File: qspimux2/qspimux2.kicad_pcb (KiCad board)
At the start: 4 copper layers, 14.2 x 23.2 mm, 13 parts, among them J101 Conn_01x10_MountingPin, J102 Conn_02x04_Odd_Even, J103 Conn_02x04_Odd_Even, U101 TS3A27518ERTWR, U102 MAX40200AUK, U103 MAX40200AUK

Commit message: qspimux2: rename project files and fix net name bugs
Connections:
- net /IO0_DO_FLASH renamed /IO1_DO_FLASH

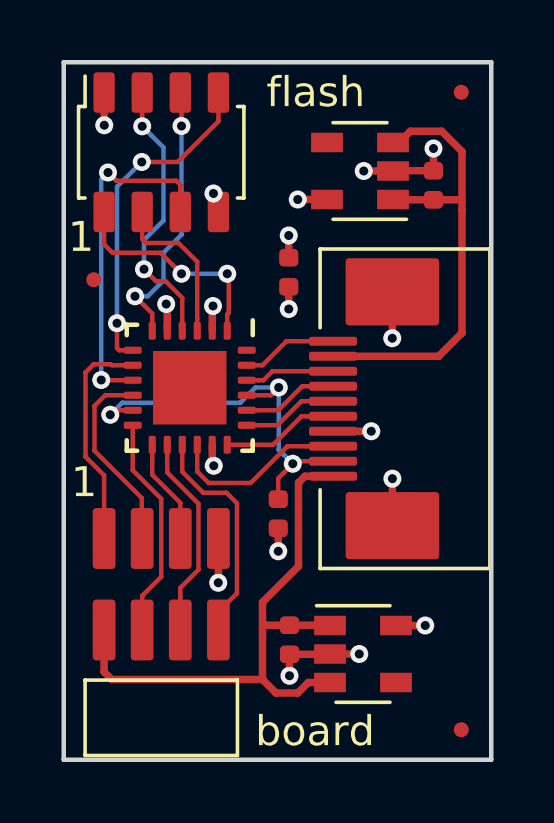
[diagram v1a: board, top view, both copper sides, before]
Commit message: qspimux2: slighty optimize board layout
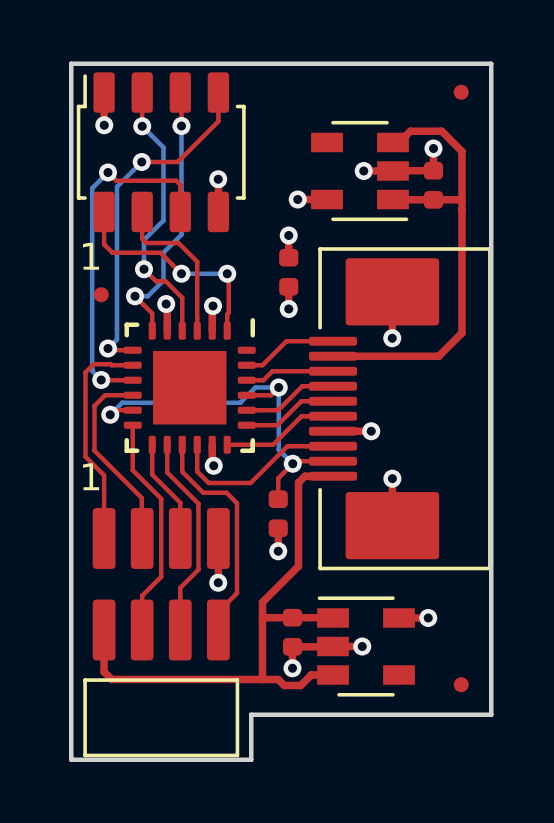
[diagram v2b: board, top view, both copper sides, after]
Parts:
- moved REF** 1.50 mm to (104.2, 68.0)
- moved REF** 0.56 mm to (92.2, 55.0)
- moved U102 0.27 mm to (101.1, 66.7)
- moved C102 0.27 mm to (98.6, 66.2)
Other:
- board size 14.2 x 23.2 mm -> 14 x 23.2 mm

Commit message: qspimux2: rename connectors to match the actual part numbers
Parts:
- J102: footprint qspimux-footprints:CLP-104-02-F-DH-A -> qspimux-footprints:CLP-104-02-F-DH
- J103: footprint qspimux-footprints:FTSH-104-01-F-DH-A -> qspimux-footprints:FTSH-104-01-F-DH
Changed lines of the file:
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@@
     (add_net GND)
   )
-  (module qspimux-footprints:CLP-104-02-F-DH-A (layer F.Cu)
+  (module qspimux-footprints:CLP-104-02-F-DH (layer F.Cu)
     (at 94.25 50.25 180)
     (fp_text reference J102 (at 0 -3.81 180) (layer F.Fab)
@@
       (net 1 GND))
   )
-  (module qspimux-footprints:FTSH-104-01-F-DH-A (layer F.Cu)
+  (module qspimux-footprints:FTSH-104-01-F-DH (layer F.Cu)
     (at 94.25 64.65 180)
     (fp_text reference J103 (at 0 3.81 180) (layer F.Fab)

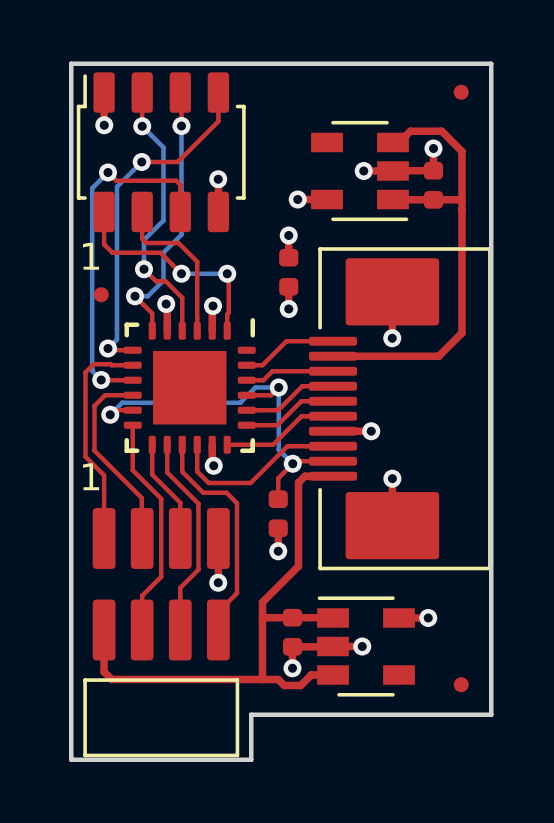
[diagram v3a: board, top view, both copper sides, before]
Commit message: improve qspimux2 manufacturability
move the vias to the ground planes a bit away from the components
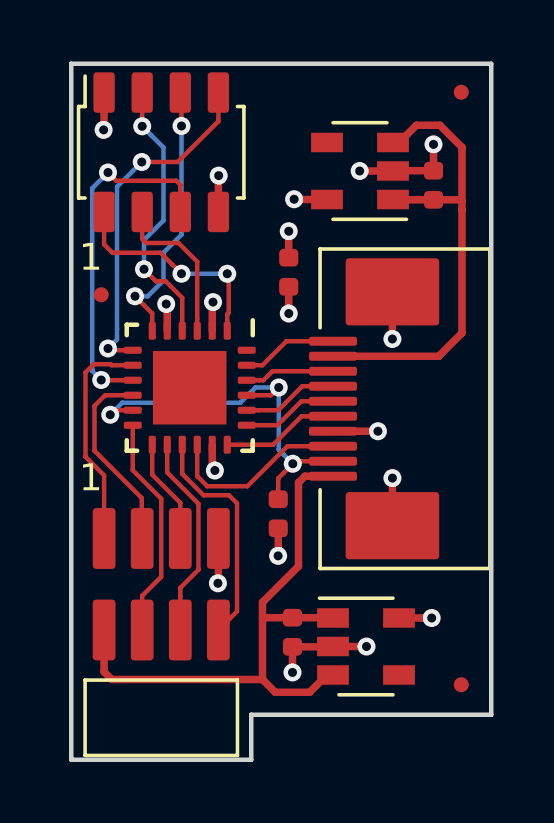
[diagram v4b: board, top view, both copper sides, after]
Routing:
- net GND: track 15.4 -> 16.8 mm
- net /VCC_FLASH: track 5.45 -> 6.16 mm
